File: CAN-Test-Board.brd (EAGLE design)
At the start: 52.3 x 59.4 mm, 52 parts, among them Y1 ECS-80-S-4X, Y2 ECS-80-S-4X

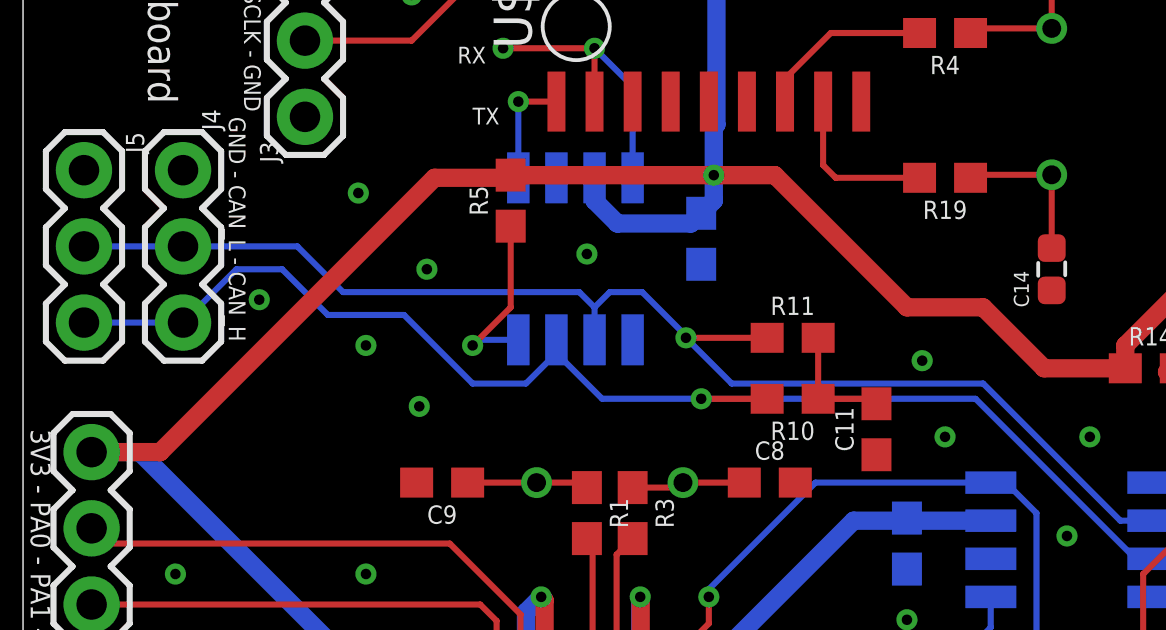
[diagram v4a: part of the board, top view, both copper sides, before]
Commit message: little better CAN trace routing around PI transceiver
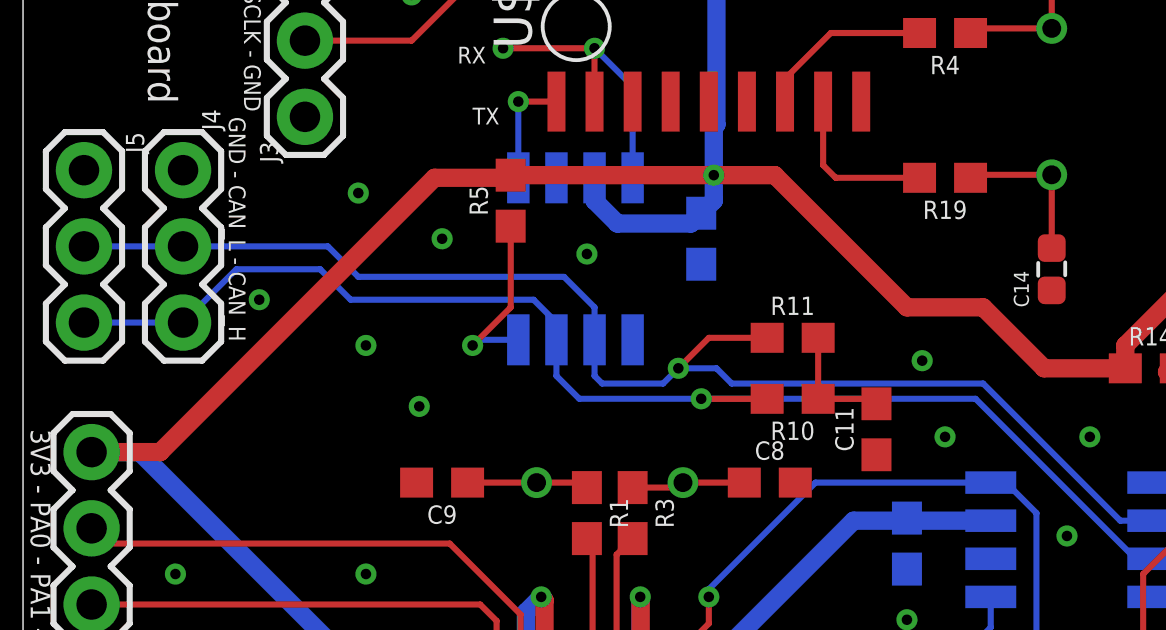
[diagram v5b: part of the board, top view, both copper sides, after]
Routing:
- net CAN_L: track 85.5 -> 86.4 mm
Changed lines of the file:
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@@
 <via x="11.43" y="26.416" extent="1-16" drill="0.35"/>
 <via x="18.796" y="37.084" extent="1-16" drill="0.35"/>
-<via x="13.462" y="36.576" extent="1-16" drill="0.35"/>
+<via x="13.97" y="37.592" extent="1-16" drill="0.35"/>
 <via x="7.874" y="35.56" extent="1-16" drill="0.35"/>
 <via x="11.43" y="34.036" extent="1-16" drill="0.35"/>
@@
 <contactref element="J5" pad="3"/>
 <wire x1="5.334" y1="34.798" x2="2.032" y2="34.798" width="0.2032" layer="16"/>
-<wire x1="22.606" y1="32.258" x2="19.304" y2="32.258" width="0.2032" layer="16"/>
-<wire x1="19.304" y1="32.258" x2="17.78" y2="33.782" width="0.2032" layer="16"/>
-<wire x1="17.78" y1="34.224" x2="17.78" y2="33.782" width="0.2032" layer="16"/>
-<wire x1="17.78" y1="33.782" x2="16.764" y2="32.766" width="0.2032" layer="16"/>
-<wire x1="16.764" y1="32.766" x2="14.986" y2="32.766" width="0.2032" layer="16"/>
+<wire x1="22.606" y1="32.258" x2="18.542" y2="32.258" width="0.2032" layer="16"/>
+<wire x1="18.542" y1="32.258" x2="17.78" y2="33.02" width="0.2032" layer="16"/>
+<wire x1="17.78" y1="34.224" x2="17.78" y2="33.02" width="0.2032" layer="16"/>
 <wire x1="7.112" y1="36.576" x2="5.334" y2="34.798" width="0.2032" layer="16"/>
-<wire x1="14.986" y1="32.766" x2="12.7" y2="35.052" width="0.2032" layer="16"/>
-<wire x1="12.7" y1="35.052" x2="10.16" y2="35.052" width="0.2032" layer="16"/>
-<wire x1="10.16" y1="35.052" x2="8.636" y2="36.576" width="0.2032" layer="16"/>
-<wire x1="8.636" y1="36.576" x2="7.112" y2="36.576" width="0.2032" layer="16"/>
+<wire x1="9.906" y1="36.576" x2="10.922" y2="35.56" width="0.2032" layer="16"/>
+<wire x1="9.906" y1="36.576" x2="7.112" y2="36.576" width="0.2032" layer="16"/>
 <wire x1="47.752" y1="24.638" x2="49.784" y2="22.606" width="0.2032" layer="1"/>
 <contactref element="U$4" pad="2"/>
@@
 <wire x1="37.846" y1="8.636" x2="37.846" y2="23.368" width="0.2032" layer="16"/>
 <wire x1="37.846" y1="23.368" x2="39.37" y2="24.892" width="0.2032" layer="16"/>
+<wire x1="17.018" y1="35.56" x2="17.78" y2="34.798" width="0.2032" layer="16"/>
+<wire x1="17.78" y1="34.798" x2="17.78" y2="34.224" width="0.2032" layer="16"/>
+<wire x1="10.922" y1="35.56" x2="17.018" y2="35.56" width="0.2032" layer="16"/>
 </signal>
 <signal name="CAN_L" class="1">
@@
 <wire x1="39.37" y1="28.448" x2="39.624" y2="28.702" width="0.2032" layer="16"/>
 <wire x1="39.624" y1="28.702" x2="40.806" y2="28.702" width="0.2032" layer="16"/>
-<via x="22.098" y="34.29" extent="1-16" drill="0.35"/>
-<wire x1="22.098" y1="34.29" x2="24.804" y2="34.29" width="0.2032" layer="1"/>
-<wire x1="32.004" y1="32.766" x2="23.622" y2="32.766" width="0.2032" layer="16"/>
-<wire x1="23.622" y1="32.766" x2="22.098" y2="34.29" width="0.2032" layer="16"/>
+<wire x1="23.622" y1="32.766" x2="32.004" y2="32.766" width="0.2032" layer="16"/>
 <wire x1="37.658" y1="28.194" x2="36.576" y2="28.194" width="0.2032" layer="16"/>
 <wire x1="36.576" y1="28.194" x2="32.004" y2="32.766" width="0.2032" layer="16"/>
@@
 <wire x1="5.334" y1="37.338" x2="2.032" y2="37.338" width="0.2032" layer="16"/>
 <wire x1="19.05" y1="34.224" x2="19.05" y2="35.306" width="0.2032" layer="16"/>
-<wire x1="19.05" y1="35.306" x2="19.558" y2="35.814" width="0.2032" layer="16"/>
-<wire x1="22.098" y1="34.29" x2="22.098" y2="34.35605" width="0.2032" layer="16"/>
-<wire x1="22.098" y1="34.35605" x2="20.64005" y2="35.814" width="0.2032" layer="16"/>
-<wire x1="19.558" y1="35.814" x2="20.64005" y2="35.814" width="0.2032" layer="16"/>
-<wire x1="19.05" y1="35.306" x2="18.542" y2="35.814" width="0.2032" layer="16"/>
-<wire x1="9.144" y1="37.338" x2="5.334" y2="37.338" width="0.2032" layer="16"/>
-<wire x1="18.542" y1="35.814" x2="10.668" y2="35.814" width="0.2032" layer="16"/>
-<wire x1="10.668" y1="35.814" x2="9.144" y2="37.338" width="0.2032" layer="16"/>
+<wire x1="19.05" y1="35.306" x2="18.034" y2="36.322" width="0.2032" layer="16"/>
+<wire x1="10.16" y1="37.338" x2="5.334" y2="37.338" width="0.2032" layer="16"/>
+<wire x1="18.034" y1="36.322" x2="11.176" y2="36.322" width="0.2032" layer="16"/>
+<wire x1="11.176" y1="36.322" x2="10.16" y2="37.338" width="0.2032" layer="16"/>
 <contactref element="U$4" pad="3"/>
 <wire x1="35.652" y1="3.296" x2="36.576" y2="4.22" width="0.2032" layer="1"/>
@@
 <wire x1="37.338" y1="26.416" x2="39.37" y2="28.448" width="0.2032" layer="1"/>
 <wire x1="37.338" y1="9.398" x2="37.338" y2="24.13" width="0.2032" layer="16"/>
+<wire x1="24.804" y1="34.29" x2="22.86" y2="34.29" width="0.2032" layer="1"/>
+<wire x1="22.86" y1="34.29" x2="21.844" y2="33.274" width="0.2032" layer="1"/>
+<via x="21.844" y="33.274" extent="1-16" drill="0.35"/>
+<wire x1="21.844" y1="33.274" x2="23.114" y2="33.274" width="0.2032" layer="16"/>
+<wire x1="23.114" y1="33.274" x2="23.622" y2="32.766" width="0.2032" layer="16"/>
+<wire x1="21.844" y1="33.274" x2="21.336" y2="32.766" width="0.2032" layer="16"/>
+<wire x1="19.304" y1="32.766" x2="19.05" y2="33.02" width="0.2032" layer="16"/>
+<wire x1="19.05" y1="33.02" x2="19.05" y2="34.224" width="0.2032" layer="16"/>
+<wire x1="21.336" y1="32.766" x2="19.304" y2="32.766" width="0.2032" layer="16"/>
 </signal>
 <signal name="N$5">

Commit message: couple part values
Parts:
- C12: value 100nF -> 0.1uF
- R14: value (none) -> 0
- R7, R9: value (none) -> 330
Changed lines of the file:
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@@
 <attribute name="VALUE" x="29.21" y="31.242" size="0.6096" layer="27" font="vector" ratio="20" rot="R90" align="top-center"/>
 </element>
-<element name="C12" library="SparkFun-Capacitors" library_urn="urn:adsk.eagle:library:510" package="0603" package3d_urn="urn:adsk.eagle:package:37414@1/1" value="100nF" x="17.78" y="50.546" smashed="yes" rot="MR90">
+<element name="C12" library="SparkFun-Capacitors" library_urn="urn:adsk.eagle:library:510" package="0603" package3d_urn="urn:adsk.eagle:package:37414@1/1" value="0.1uF" x="17.78" y="50.546" smashed="yes" rot="MR90">
 <attribute name="NAME" x="18.542" y="50.546" size="0.6096" layer="26" font="vector" ratio="20" rot="MR90" align="bottom-center"/>
 <attribute name="PROD_ID" value="CAP-07885" x="-69.85" y="147.066" size="1.778" layer="28" rot="MR90" display="off"/>
@@
 <attribute name="VALUE" x="41.656" y="25.908" size="0.6096" layer="28" font="vector" ratio="20" rot="MR0" align="top-center"/>
 </element>
-<element name="R7" library="SparkFun-Resistors" library_urn="urn:adsk.eagle:library:532" package="0603" package3d_urn="urn:adsk.eagle:package:39650/1" value=" " x="28.194" y="7.62" smashed="yes" rot="R90">
+<element name="R7" library="SparkFun-Resistors" library_urn="urn:adsk.eagle:library:532" package="0603" package3d_urn="urn:adsk.eagle:package:39650/1" value="330" x="28.194" y="7.62" smashed="yes" rot="R90">
 <attribute name="NAME" x="27.432" y="7.62" size="0.6096" layer="25" font="vector" ratio="20" rot="R90" align="bottom-center"/>
 <attribute name="PROD_ID" value=" " x="120.904" y="60.96" size="1.778" layer="27" rot="R90" display="off"/>
@@
 <attribute name="VALUE" x="41.656" y="29.464" size="0.6096" layer="28" font="vector" ratio="20" rot="MR180" align="top-center"/>
 </element>
-<element name="R9" library="SparkFun-Resistors" library_urn="urn:adsk.eagle:library:532" package="0603" package3d_urn="urn:adsk.eagle:package:39650/1" value=" " x="25.654" y="7.874" smashed="yes" rot="R90">
+<element name="R9" library="SparkFun-Resistors" library_urn="urn:adsk.eagle:library:532" package="0603" package3d_urn="urn:adsk.eagle:package:39650/1" value="330" x="25.654" y="7.874" smashed="yes" rot="R90">
 <attribute name="NAME" x="24.892" y="7.874" size="0.6096" layer="25" font="vector" ratio="20" rot="R90" align="bottom-center"/>
 <attribute name="PROD_ID" value=" " x="118.364" y="68.834" size="1.778" layer="27" rot="R90" display="off"/>
@@
 <attribute name="VALUE" x="0" y="41.148" size="0.6096" layer="27" font="vector" ratio="20" rot="R270"/>
 </element>
-<element name="R14" library="SparkFun-Resistors" library_urn="urn:adsk.eagle:library:532" package="0603" package3d_urn="urn:adsk.eagle:package:39650/1" value=" " x="37.592" y="33.274" smashed="yes">
+<element name="R14" library="SparkFun-Resistors" library_urn="urn:adsk.eagle:library:532" package="0603" package3d_urn="urn:adsk.eagle:package:39650/1" value="0" x="37.592" y="33.274" smashed="yes">
 <attribute name="NAME" x="37.592" y="34.036" size="0.6096" layer="25" font="vector" ratio="20" align="bottom-center"/>
 <attribute name="PROD_ID" value=" " x="37.592" y="33.274" size="1.778" layer="27" display="off"/>

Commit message: couple changes for a possible rev 2 (led sizes, button footprint)
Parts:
- C13, C14: device Resistor_Capacitor:CAP_0603 -> SparkFun-Capacitors:0603
- C15: value 100nF -> 0.1uF
- D1, D2: value (none) -> LED-0805; device SparkFun-LED:LED-0603 -> LED-0805:0805
- RESET: value (none) -> DISCRETECOMPONENTS_SWITCH; device DiscreteComponents:SW_2512 -> Push button:DISCRETECOMPONENTS_SW_2512
- moved C11 21.3 mm to (8.64, 39.0), turned to 0 degrees
- moved R10 17.3 mm to (8.64, 35.3)
- moved R11 17.2 mm to (8.64, 37.1)
- moved R7 1.30 mm to (27.9, 8.89)
- moved R9 1.14 mm to (25.1, 8.89)
- moved R19 1.02 mm to (31.8, 39.6)
- moved D2 0.92 mm to (24.9, 4.32), turned to 90 degrees
- moved RESET 0.89 mm to (15.5, 8.00)
- moved R4 0.89 mm to (31.6, 44.5)
- moved J5 0.63 mm to (2.67, 39.9)
- moved D1 0.57 mm to (27.9, 4.32), turned to 90 degrees
- moved C17 0.38 mm to (41.1, 31.1)
- moved R14 0.38 mm to (37.2, 33.3)
- moved C8 0.25 mm to (25.1, 29.5)
- moved C13 0.13 mm to (34.3, 47.6)
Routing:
- net GND: track 10.2 -> 13.9 mm
- net 3V3: track 167.5 -> 170.0 mm
- net CAN_L: track 86.4 -> 84.5 mm, vias 4 -> 3
- net SWCLK: track 26.5 -> 25.2 mm
- net LED1: track 9.60 -> 8.37 mm
- net N$4: track 5.19 -> 4.03 mm
- net LED2: track 34.0 -> 32.9 mm
- net CAN_H: track 83.8 -> 82.9 mm, vias 3 -> 2
- net N$3: track 4.96 -> 4.05 mm
- net OSC2: track 5.88 -> 6.77 mm
- net 3V3_REG: track 4.13 -> 4.89 mm
- net OSC1: track 5.51 -> 6.23 mm
- net N$24: track 2.08 -> 2.62 mm
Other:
- board text added: "Fix header pin labels"
- board text added: "ROV CAN test board V2 - Mon Year Grant Geyer"
- board text removed: "ROV CAN test board V1 - Sep 2020 Grant Geyer"
